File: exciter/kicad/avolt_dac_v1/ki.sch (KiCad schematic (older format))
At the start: 31 parts, among them U1 MCP4822, U10 74AHC74, U2 TL052

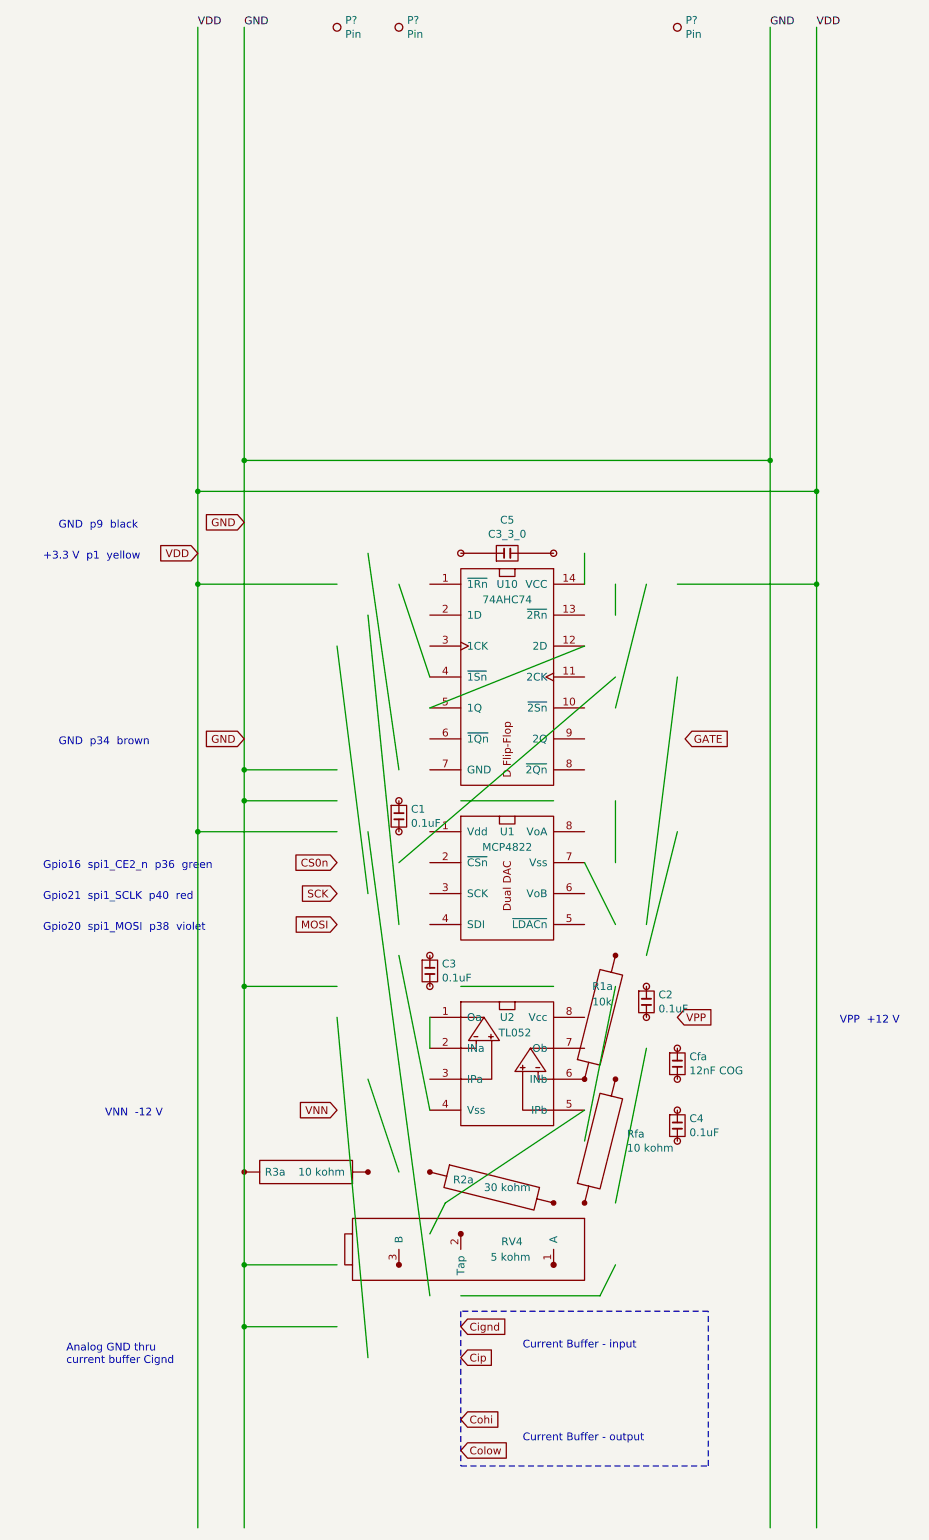
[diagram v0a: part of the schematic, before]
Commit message: Exciter:kicad:  avolt_dac_v1  Voltage DAC, v1.1
Tighten up RPi connections and VDD.  No schematic change.
Added C6 0.1 uF bypass VDD near RPi connections.
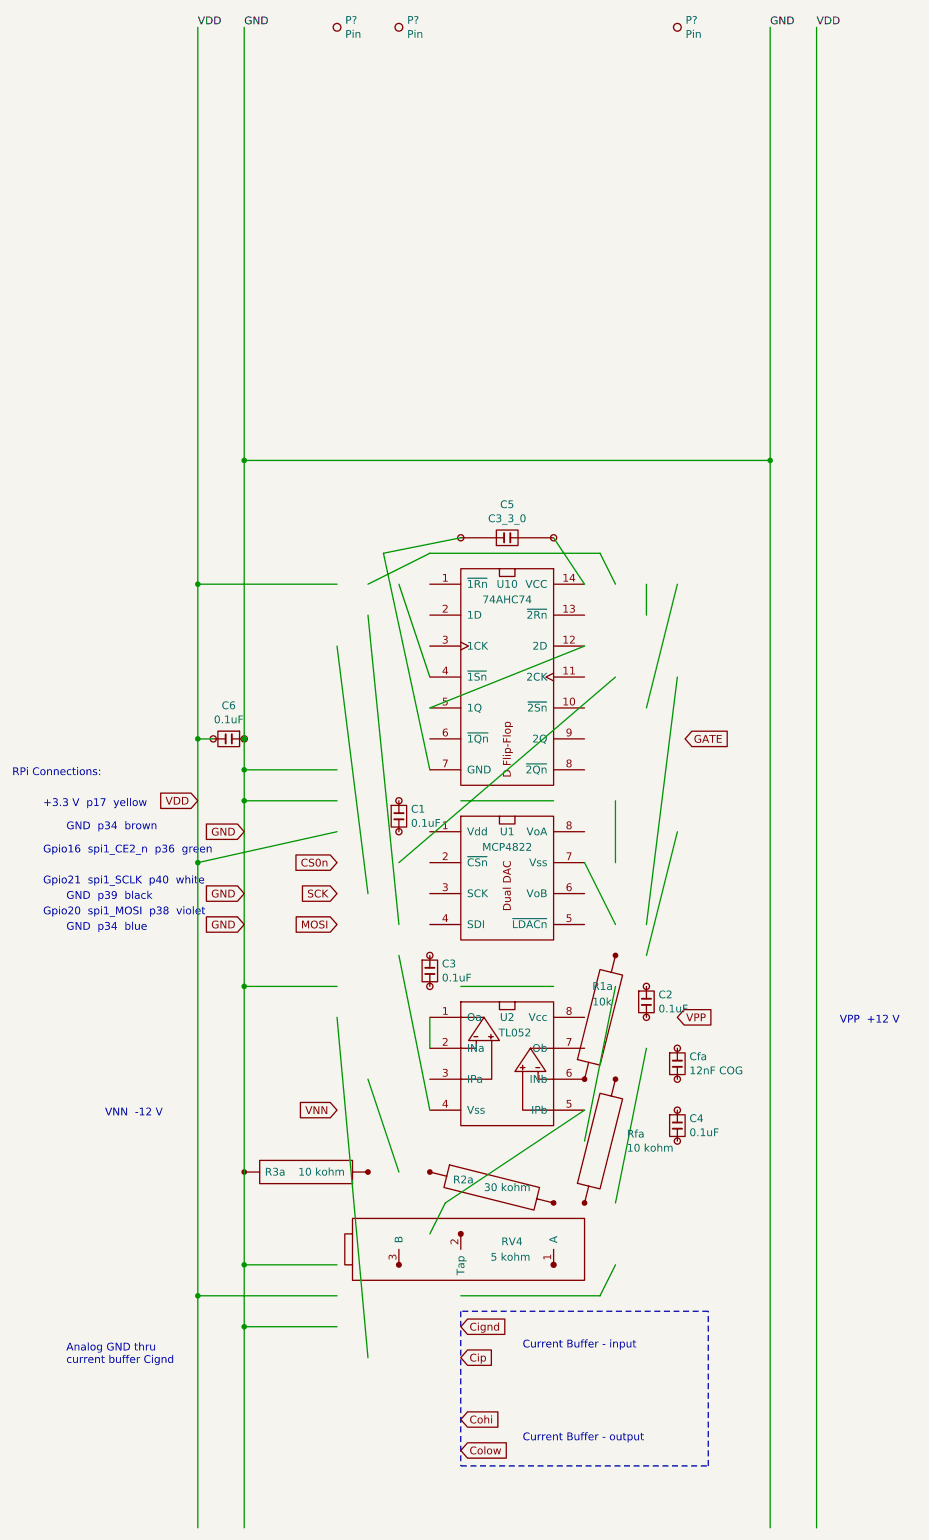
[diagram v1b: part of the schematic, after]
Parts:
- added C6: 0.1uF, symbol _Breadboard:C1_1_0
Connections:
- wire segments 119 -> 122
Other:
- note added: "+3.3 V p17 yellow"
- note added: "GND p34 blue"
- note added: "GND p39 black"
- note added: "Gpio21 spi1_SCLK p40 white"
- note added: "RPi Connections:"
- note removed: "+3.3 V p1 yellow"
- note removed: "GND p9 black"
- note removed: "Gpio21 spi1_SCLK p40 red"
- moved on the sheet: C5
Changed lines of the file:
@@
 Sheet 1 1
 Title "avolt_dac_v1/  Voltage DAC"
-Date "2022-04-04"
-Rev "v1.0"
+Date "2022-07-28"
+Rev "v1.1"
 Comp "William A. Hudson"
-Comment1 ""
+Comment1 "v1.1 - Tighten up RPi connections, VDD"
 Comment2 ""
 Comment3 ""
@@
 Wire Wire Line
 	2000 600  2000 3400
-Wire Wire Line
-	1700 600  1700 3600
-Wire Wire Line
-	5700 600  5700 3600
 $Comp
 L _Breadboard:MCP4802 U1
@@
 Wire Wire Line
 	2000 5600 2000 6800
-Wire Wire Line
-	4800 4200 5700 4200
-Connection ~ 5700 4200
-Wire Wire Line
-	2600 5800 1700 5800
-Connection ~ 1700 5800
-Wire Wire Line
-	1700 5800 1700 10300
 $Comp
 L _Breadboard:R4_4_1 R1a
@@
 Text GLabel 2600 7600 0    50   Input ~ 0
 VNN
-Text GLabel 4800 7000 2    50   Input ~ 0
-VPP
 Wire Wire Line
 	2800 6200 2600 4600
@@
 Wire Wire Line
 	3000 6000 4400 4800
-Wire Wire Line
-	4400 4400 4400 4200
-Wire Wire Line
-	4400 5000 4600 4200
 Wire Wire Line
 	3200 4800 3000 4200
@@
 	2600 4200 1700 4200
 Connection ~ 1700 4200
-Wire Wire Line
-	1700 4200 1700 5800
 Text GLabel 3400 9800 2    50   Input ~ 0
 Colow
@@
 L _Breadboard:C3_3_0 C5
 U 1 1 624E6C27
-P 3700 4000
-F 0 "C5" V 3915 4000 50  0000 C CNN
-F 1 "C3_3_0" V 3824 4000 50  0000 C CNN
-F 2 "" H 3700 4000 50  0001 C CNN
-F 3 "" H 3700 4000 50  0001 C CNN
-	1    3700 4000
+P 3700 3900
+F 0 "C5" V 3915 3900 50  0000 C CNN
+F 1 "C3_3_0" V 3824 3900 50  0000 C CNN
+F 2 "" H 3700 3900 50  0001 C CNN
+F 3 "" H 3700 3900 50  0001 C CNN
+	1    3700 3900
 	0    -1   -1   0
 $EndComp
 Wire Wire Line
-	3000 5400 2800 4000
-Wire Wire Line
-	4200 4000 4200 4200
-Wire Wire Line
-	5700 4200 5700 10300
+	4000 3900 4200 4200
 Wire Wire Line
 	4400 8600 4300 8800
@@
 	4300 8800 3400 8800
 Wire Wire Line
-	2800 5800 3200 8800
-Wire Wire Line
 	3000 8000 2800 7400
-Wire Wire Line
-	1700 3600 5700 3600
-Connection ~ 1700 3600
-Wire Wire Line
-	1700 3600 1700 4200
-Connection ~ 5700 3600
-Wire Wire Line
-	5700 3600 5700 4200
 Wire Wire Line
 	5400 600  5400 3400
@@
 Connection ~ 2000 3400
 Wire Wire Line
-	2000 3400 2000 5400
+	2000 3400 2000 5200
 Connection ~ 5400 3400
 Wire Wire Line
 	5400 3400 5400 10300
-Text GLabel 2000 3800 0    50   Input ~ 0
-GND
-Text GLabel 1700 4000 0    50   Input ~ 0
+Text GLabel 1700 5600 0    50   Input ~ 0
 VDD
-Text Notes 700  6450 0    50   ~ 0
+Text Notes 700  6350 0    50   ~ 0
 Gpio20  spi1_MOSI  p38  violet
-Text Notes 700  6250 0    50   ~ 0
-Gpio21  spi1_SCLK  p40  red
-Text Notes 700  6050 0    50   ~ 0
+Text Notes 700  6150 0    50   ~ 0
+Gpio21  spi1_SCLK  p40  white
+Text Notes 700  5950 0    50   ~ 0
 Gpio16  spi1_CE2_n  p36  green
-Text Notes 800  3850 0    50   ~ 0
-GND  p9  black
-Text Notes 700  4050 0    50   ~ 0
-+3.3 V  p1  yellow
+Text Notes 700  5650 0    50   ~ 0
++3.3 V  p17  yellow
 Text Notes 5850 7050 0    50   ~ 0
 VPP  +12 V
@@
 Text GLabel 4850 5200 2    50   Input ~ 0
 GATE
-Text Notes 800  5250 0    50   ~ 0
+Text Notes 850  5800 0    50   ~ 0
 GND  p34  brown
-Text GLabel 2000 5200 0    50   Input ~ 0
+Text GLabel 2000 5800 0    50   Input ~ 0
 GND
 Wire Wire Line
@@
 Wire Notes Line
 	5000 8900 3400 8900
+Wire Wire Line
+	3200 5400 2900 4000
+Wire Wire Line
+	2900 4000 3400 3900
+Wire Wire Line
+	4600 5000 4800 4200
+Wire Wire Line
+	4600 4400 4600 4200
+Wire Wire Line
+	4400 4200 4300 4000
+Wire Wire Line
+	4300 4000 3200 4000
+Wire Wire Line
+	3200 4000 2800 4200
+Wire Wire Line
+	2600 8800 1700 8800
+Connection ~ 1700 8800
+Wire Wire Line
+	1700 8800 1700 10300
+Text GLabel 2000 6200 0    50   Input ~ 0
+GND
+Text Notes 850  6250 0    50   ~ 0
+GND  p39  black
+Text GLabel 4800 7000 2    50   Input ~ 0
+VPP
+Text GLabel 2000 6400 0    50   Input ~ 0
+GND
+Text Notes 850  6450 0    50   ~ 0
+GND  p34  blue
+Wire Wire Line
+	1700 4200 1700 5200
+Wire Wire Line
+	2600 5800 1700 6000
+Connection ~ 1700 6000
+Wire Wire Line
+	1700 6000 1700 8800
+Text Notes 500  5450 0    50   ~ 0
+RPi Connections:
+Wire Wire Line
+	1700 600  1700 4200
+Wire Wire Line
+	5700 600  5700 10300
+$Comp
+L _Breadboard:C1_1_0 C6
+U 1 1 62E754B5
+P 1900 5200
+F 0 "C6" V 1685 5200 50  0000 C CNN
+F 1 "0.1uF" V 1776 5200 50  0000 C CNN
+F 2 "" H 1900 5200 50  0001 C CNN
+F 3 "" H 1900 5200 50  0001 C CNN
+	1    1900 5200
+	0    1    1    0
+$EndComp
+Connection ~ 2000 5200
+Wire Wire Line
+	2000 5200 2000 5400
+Wire Wire Line
+	1800 5200 1700 5200
+Connection ~ 1700 5200
+Wire Wire Line
+	1700 5200 1700 6000
 $EndSCHEMATC
